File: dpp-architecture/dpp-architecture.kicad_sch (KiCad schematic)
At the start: 4 parts

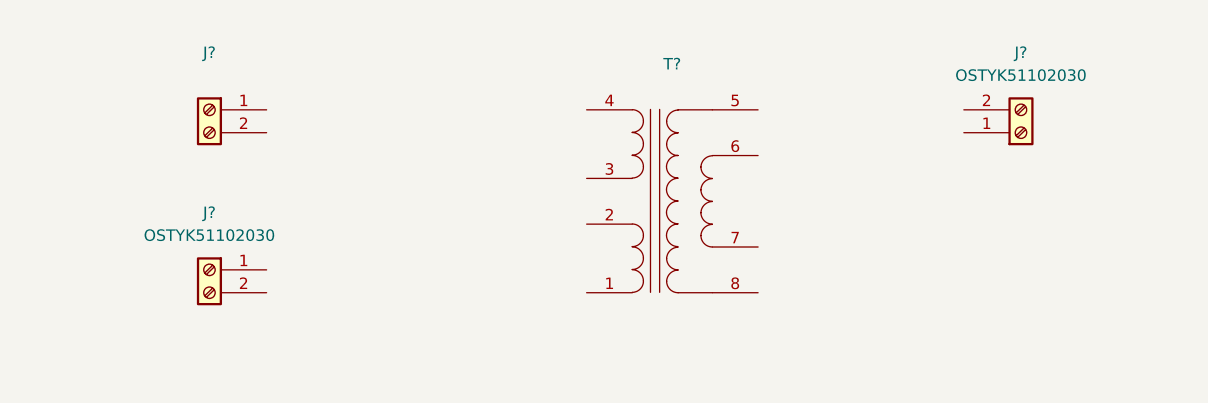
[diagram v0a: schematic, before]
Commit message: Added mosfet, primary and secondary capacitors and a snubber capacitor
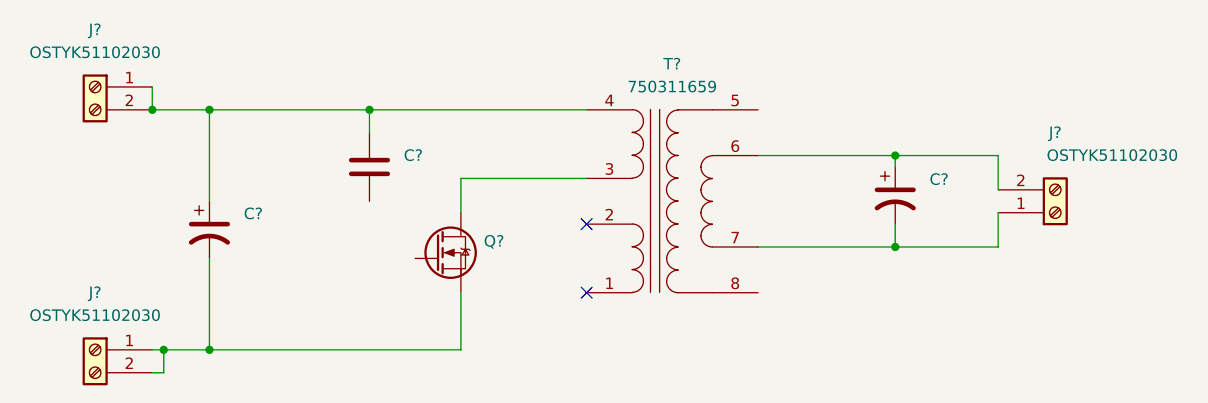
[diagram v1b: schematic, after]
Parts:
- added C? (x2): (no value), symbol C-2200uF-50V-20%:2200
- added C?: (no value), symbol C-47pF-0805-100V-5%:47pF
- added Q?: (no value), symbol Q-IRFU120NPBF:IRFU120NPBF
- J?: value (none) -> OSTYK51102030; footprint (none) -> J-OSTYK51102030:OSTYK51102030
- T?: value (none) -> 750311659; footprint (none) -> T-750311659:750311659
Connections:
- net at T?.3 (PRI_1): now also Q?.2 (D), Q?.4 (D)
- net at T?.4 (PRI_2): now also J?.1, J?.2, C?.1, C?.1
- net at T?.6 (SEC_2): now also J?.2, C?.1
- net at T?.7 (SEC_3): now also J?.1, C?.2
- net at J?.1: now also J?.2, C?.2, Q?.3 (S)
- no-connect marks 0 -> 2
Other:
- moved on the sheet: J?

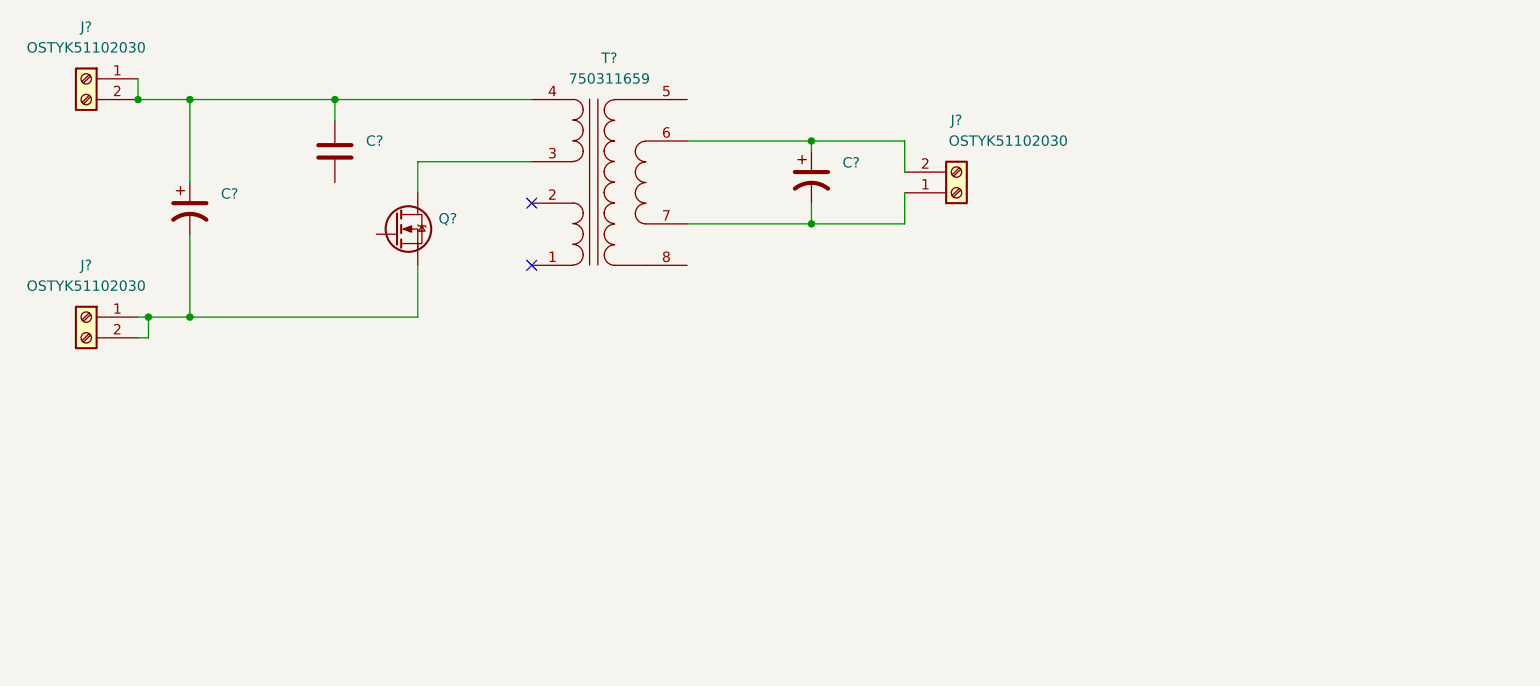
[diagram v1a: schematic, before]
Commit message: Finished schematic and pcb routing, created images of the 3D model
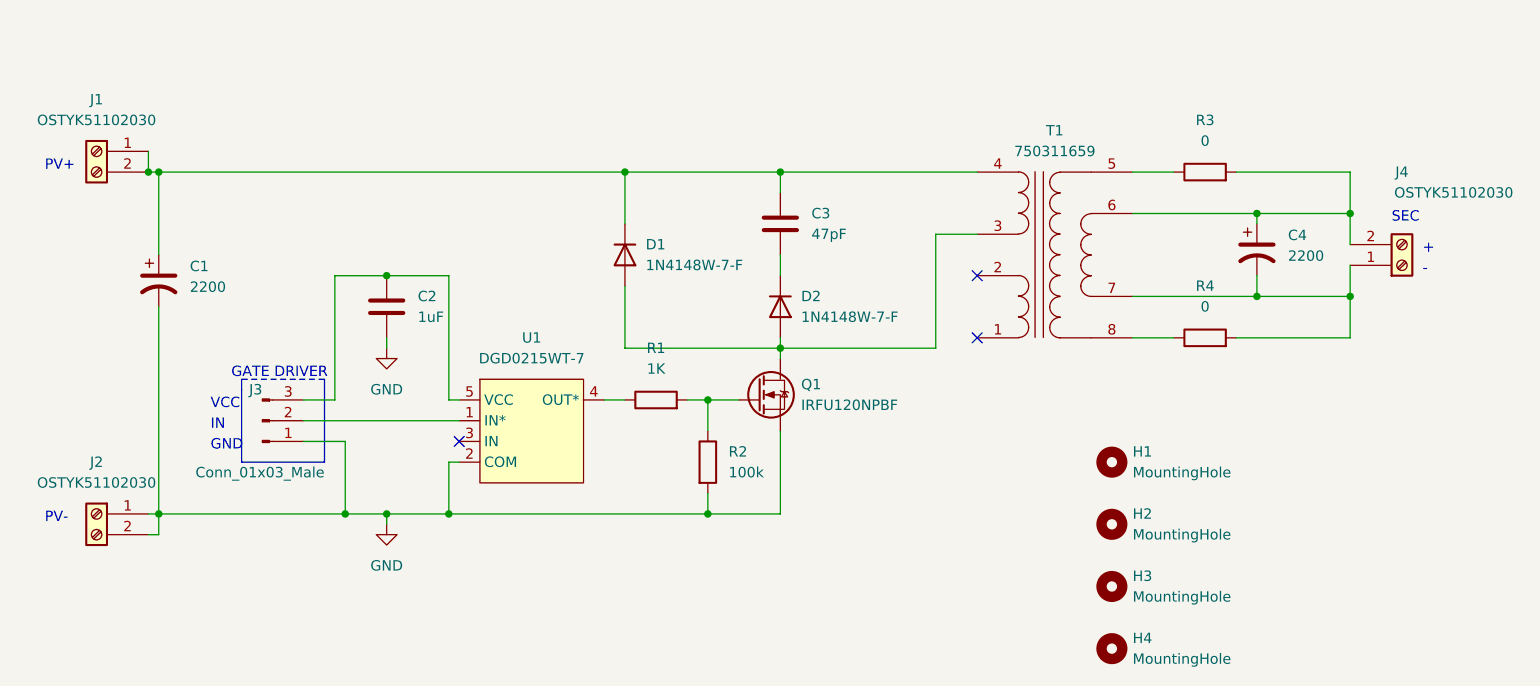
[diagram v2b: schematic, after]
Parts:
- added C2: 1uF, Capacitor_SMD:C_0805_2012Metric, symbol C-1uF-0805:1uF
- added D1, D2: 1N4148W-7-F, Diode_SMD:D_SOD-123, symbol D-1N4148W-7-F:1N4148W-7-F
- added H1, H2, H3, H4: MountingHole, MountingHole:MountingHole_3.5mm, symbol Mechanical:MountingHole
- added J3: Conn_01x03_Male, Connector_PinHeader_2.54mm:PinHeader_1x03_P2.54mm_Vertical, symbol Connector:Conn_01x03_Male
- added R1: 1K, Resistor_SMD:R_0805_2012Metric, symbol R-1K-0805:1K
- added R2: 100k, Resistor_SMD:R_0805_2012Metric_Pad1.20x1.40mm_HandSolder, symbol R-100K-0805:100k
- added R3, R4: 0, Resistor_SMD:R_0805_2012Metric, symbol R-0-0805:0
- added U1: DGD0215WT-7, Package_TO_SOT_SMD:SOT-23-5_HandSoldering, symbol U-DGD0215WT-7:DGD0215WT-7
- C1, C4: renamed from C?; value (none) -> 2200; footprint (none) -> Capacitor_THT:CP_Radial_D16.0mm_P7.50mm
- C3: renamed from C?; value (none) -> 47pF; footprint (none) -> Capacitor_SMD:C_0805_2012Metric
- Q1: renamed from Q?; value (none) -> IRFU120NPBF; footprint (none) -> Package_TO_SOT_THT:TO-251-3-1EP_Horizontal_TabDown
- gave numbers to parts that had none: 4
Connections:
- net at Q1.2 (D), Q1.4 (D), T1.3 (PRI_1): now also D1.2 (A), D2.2 (A)
- net at C1.1, C3.1, J1.1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: now also D1.1 (K)
- net at T1.5 (SEC_1): now also R3.1
- net at C4.1, J4.2, T1.6 (SEC_2): now also R3.2
- net at C4.2, J4.1, T1.7 (SEC_3): now also R4.2
- net at T1.8 (SEC_4): now also R4.1
- net GND: now reaches C1.2, J2.1, J2.2, Q1.3 (S)
- net GND: now also C2.2, J3.1 (Pin_1), R2.2, U1.2 (COM)
- net at Q1.1 (G): now also R1.2, R2.1
- net at C3.2: now also D2.1 (K)
- new net: J3.2 (Pin_2), U1.1 (IN*)
- new net: C2.1, J3.3 (Pin_3), U1.5 (VCC)
- new net: R1.1, U1.4 (OUT*)
- no-connect marks 2 -> 3
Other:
- note added: "+"
- note added: "-"
- note added: "GATE DRIVER"
- note added: "GND"
- note added: "IN"
- note added: "PV+"
- note added: "PV-"
- note added: "SEC"
- note added: "VCC"
- title: (none) -> DPP Architecture for an MPPT design - Leonardo Ward
- moved on the sheet: C1, C3, C4, J1, J2, J4, Q1, T1
